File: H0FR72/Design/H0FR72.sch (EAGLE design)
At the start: 38 parts, among them P2 HEXABIT_17.32_NO_P6_P7_P12, Q2 STD36P4LLF6, Q3 MMBT3904LT1, U1 STM32G0B1CEU6NUFQFPN48_STM32_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, U2 INA199A2DCKT, U3 PMD3001D,115, X1 XTALL_CSTCE8M00G52

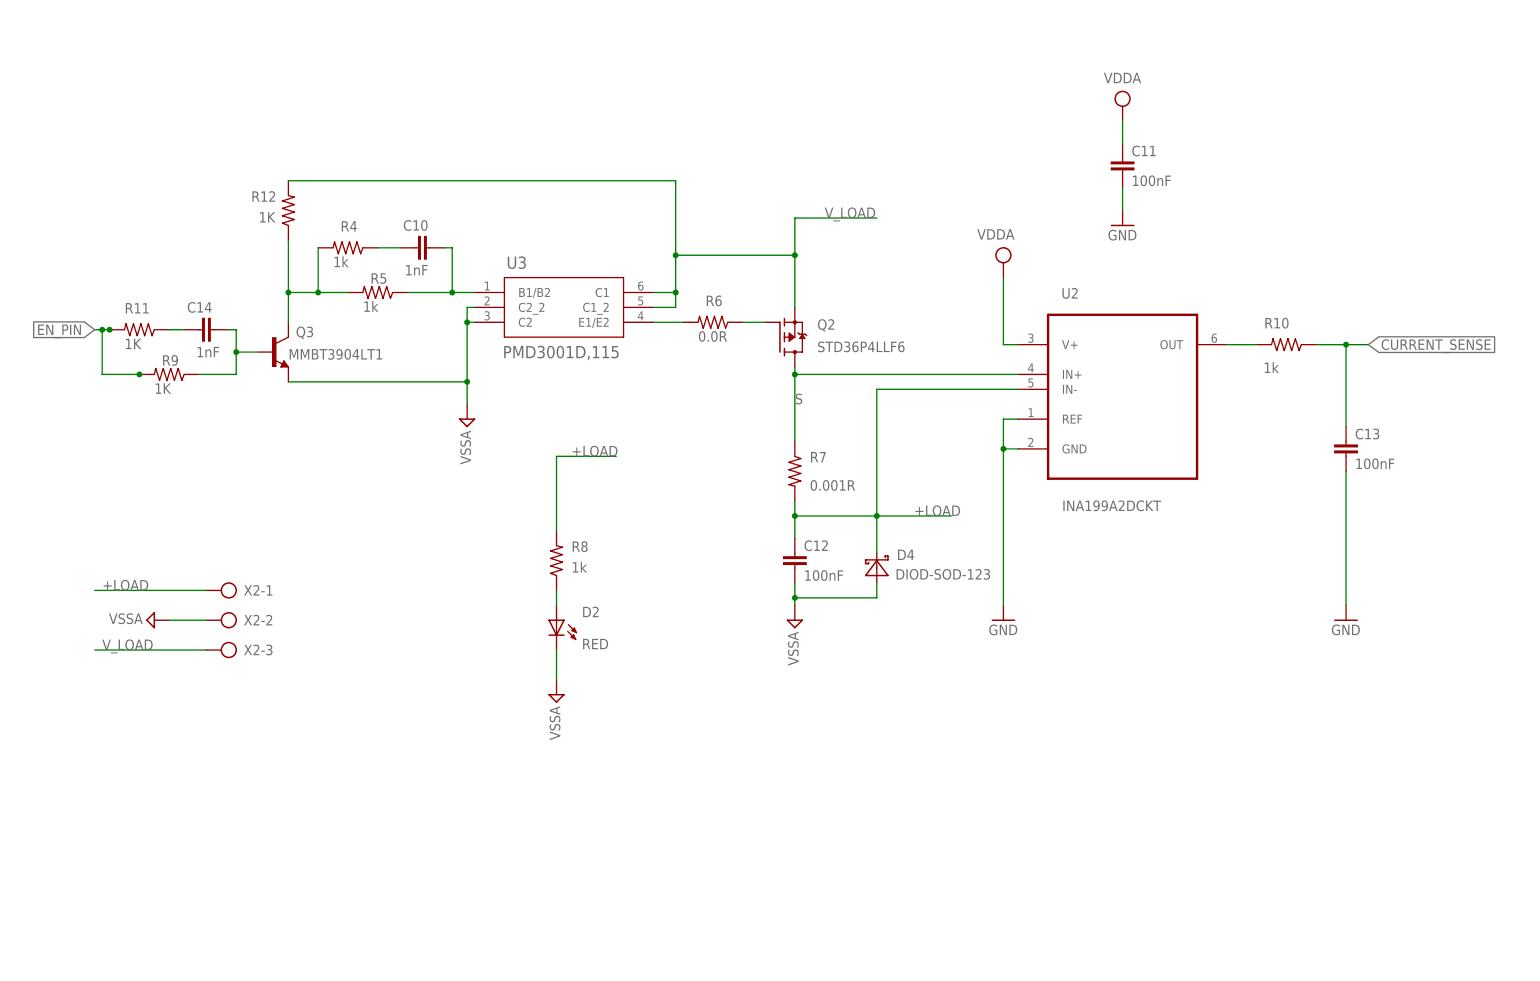
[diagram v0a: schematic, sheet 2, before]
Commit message: -Update the electronic & layout designs to improve the performance (the BOM have been changed too) .
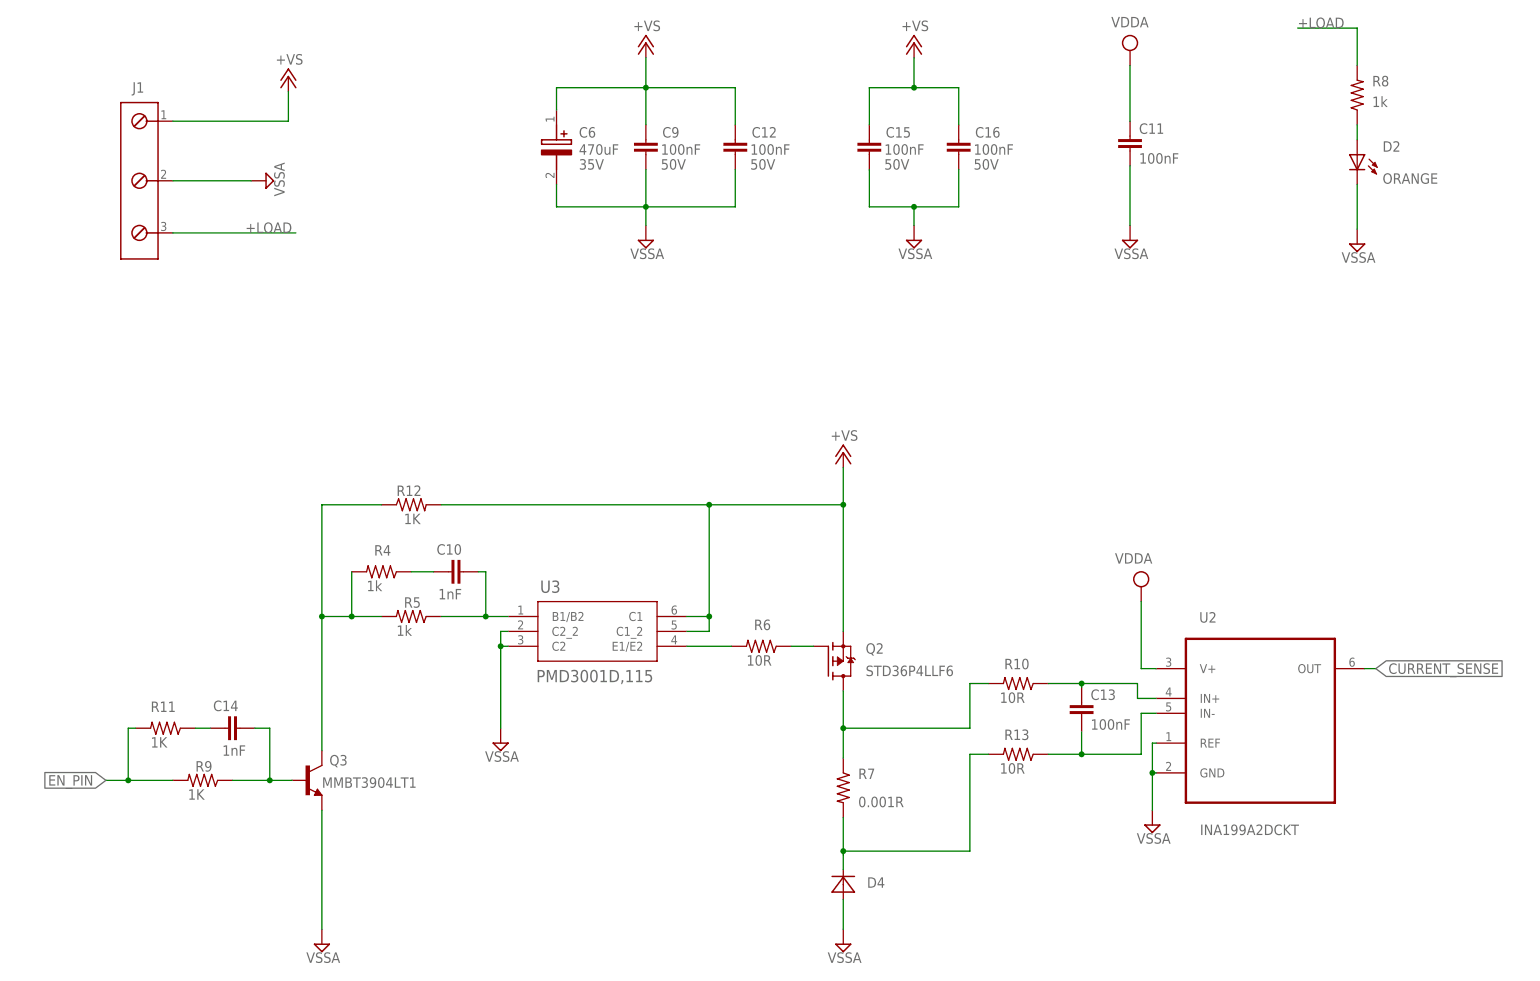
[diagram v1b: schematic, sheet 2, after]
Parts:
- removed JP2: (no value), pinhead:PINHD-1X3
- removed X2: (no value), HEXABITZ_CONNECTION_PARTS:AK500/3
- added C15, C16, C9: (no value), HEXABITZ_RCLS:C-0402
- added C6: ESH477M035AH3AA, HEXABITZ_RCLS:ESH477M035AH3AA
- added J1: (no value), HEXABITZ_CONNECTION_PARTS:691213710003
- added R13: 10R, HEXABITZ_RCLS:R-0402
- added SWD: (no value), HEXABITZ_CONNECTION_PARTS:PINHD-1X3SWD
- C1, C10, C11, C14, C3, C5, C8: device HEXABITZ_RCLS:C-0603 -> HEXABITZ_RCLS:C-0402
- C12: value 100nF -> (none); device HEXABITZ_RCLS:C-0603 -> HEXABITZ_RCLS:C-0402; MFN KEMET -> (none); MPN C0603C104K8RACTU -> (none); OCTOPART_URL https://octopart.com/c0603c104k8ractu-kemet-145075?r=sp&s=9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 -> (none); TOLERANCE 10% -> (none); VOLTAGE_RATING 10V -> 50V
- C13: device HEXABITZ_RCLS:C-0603 -> HEXABITZ_RCLS:C-0402; TOLERANCE 10% -> 10V; VOLTAGE_RATING 10V -> 10%
- C2, C4, C7: device HEXABITZ_RCLS:C-0805-POL -> HEXABITZ_RCLS:C-0603-POL
- D2: value RED -> ORANGE
- R1, R11, R12, R2, R3, R4, R5, R8, R9: device HEXABITZ_RCLS:R-0603 -> HEXABITZ_RCLS:R-0402
- R10: value 1k -> 10R; device HEXABITZ_RCLS:R-0603 -> HEXABITZ_RCLS:R-0402; TOLERANCE 5% -> 1%
- R6: value 0.0R -> 10R; device HEXABITZ_RCLS:R-0603 -> HEXABITZ_RCLS:R-0402
- R7: device HEXABITZ_RCLS:R-US_R2512 -> HEXABITZ_RCLS:R_1206R1206; MPN (none) -> PA1206FRM470R01L
- RESET: value (none) -> R
- U1: value STM32G0B1CEU6NUFQFPN48_STM32_STM -> STM32G0B1CEU6N; device HEXABITZ_ICs:STM32G0B1CEU6NUFQFPN48_STM32_STM -> HEXABITZ_ICs:STM32G0B1CEU6N
- U3: device PMD3001D,115:PMD3001DSOT457_NEX -> HEXABITZ_ICs:PMD3001DSOT457_NEX
- renumbered R to RESET
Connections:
- removed net AGND: C1.2, C12.2, C2.-, C5.2, C7.-, D2.C, D4.A, Q3.E, R2.2, U1.VSS/VSSA, U3.C2, U3.C2_2, X2-2.KL
- removed net N$9: R10.2, U2.OUT
- removed net S: Q2.D, R7.1, U2.IN+
- removed net UART4_RX: P2.SD1, U1.PA1
- removed net UART4_TX: P2.SU1, U1.PA0
- removed net V_LOAD: Q2.S, R12.2, U3.C1, U3.C1_2, X2-3.KL
- new net +VS: C12.2, C15.2, C16.2, C6.+, C9.2, J1.1, Q2.S, R12.2, U3.C1, U3.C1_2
- new net CS: Q2.D, R10.2, R7.1
- new net N$11: C13.1, R10.1, U2.IN+
- new net N$18: C13.2, R13.1, U2.IN-
- new net UART1_RX: P2.SD2, U1.PA9
- new net UART1_TX: P2.SU2, U1.PA10
- new net VREF: C1.1, C2.1, U1.VREF+
- new net VSSA: C1.2, C11.2, C12.1, C15.1, C16.1, C2.2, C5.2, C6.-, C7.2, C9.1, D2.C, D4.A, J1.2, Q3.E, R2.2, U1.VSS/VSSA, U2.GND, U2.REF, U3.C2, U3.C2_2
- net +LOAD: now also J1.3, R13.2; no longer C12.1, U2.IN-, X2-1.KL
- net CLK: now also SWD.1, SWD.2; no longer JP2.1, JP2.2
- net CURRENT_SENSE: now also U1.PA0, U2.OUT; no longer C13.1, R10.1, U1.PB12
- net DATA: now also SWD.3; no longer JP2.3
- net EN_PIN: now also U1.PD1; no longer U1.PB6
- net GND: now also C4.2, U1.PB12, U1.PB13; no longer C11.2, C13.2, C4.-, U1.PB0, U1.PB1, U1.PB7, U1.PB8, U1.PB9, U2.GND, U2.REF
- net N$3: now also U1.PA4; no longer U1.PB13
- net UART2_RX: now also P2.SD5; no longer P2.SD2
- net UART2_TX: now also P2.SU5; no longer P2.SU2
- net UART3_RX: now also P2.SD1; no longer P2.SD4
- net UART3_TX: now also P2.SU1; no longer P2.SU4
- net UART5_RX: now also P2.SD3; no longer P2.SD5
- net UART5_TX: now also P2.SU3; no longer P2.SU5
- net UART6_RX: now also P2.SD4, U1.PB9; no longer P2.SD3, U1.PA5
- net UART6_TX: now also P2.SU4, U1.PB8; no longer P2.SU3, U1.PA4
- net VDD: now also C4.1; no longer C4.+
- net VDDA: now also C7.1; no longer C1.1, C2.+, C7.+, U1.VBAT, U1.VREF+
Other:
- note added: "Current-Shunt Monitor"
- note added: "Driver Output Led_Ind"
- note added: "Driver Power Coupling"
- note added: "Gain = 100 V/V Gain Error = 0.89%"
- note added: "H0FR72"
- note added: "H0FR72_Backend"
- note added: "H0FR72_Frontend"
- note added: "Input Power Coupling"
- note added: "Load driver"
- note added: "U2 Coupling"
- note added: "VS=(3.3-18) Volts"
- note removed: "H0FR71"
- note removed: "H0FR71_Backend"
- note removed: "H0FR71_Frontend"
- note removed: "V_load=(3.3-18)"
- moved on the sheet: C10, C11, C12, C13, C14, D1, D2, Q2, Q3, R1, R10, R11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

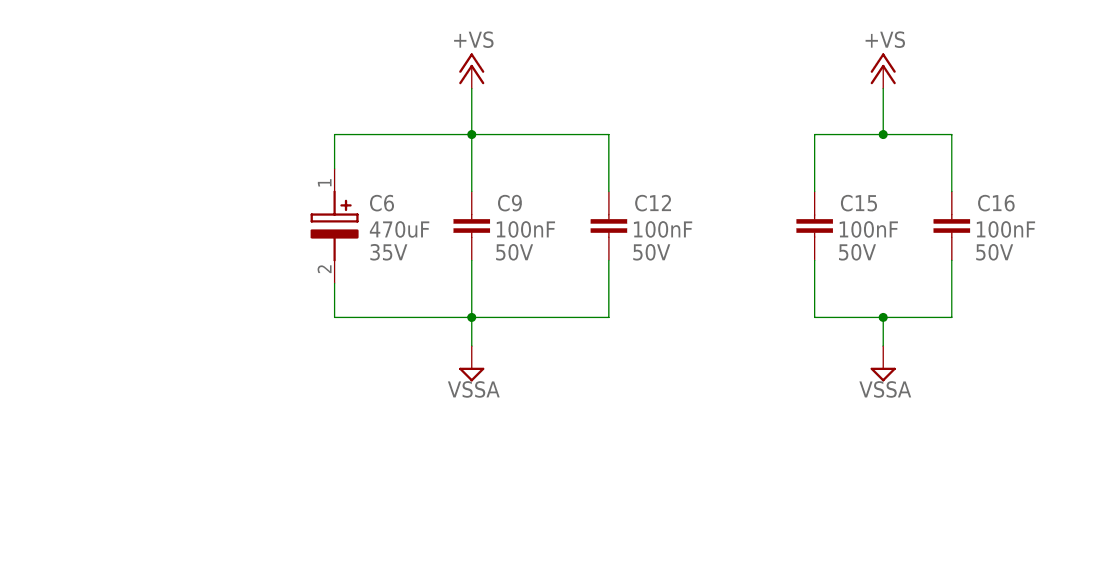
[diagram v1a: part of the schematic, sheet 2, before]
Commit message: -Add additional 10u capacitor to gate driver IC supply
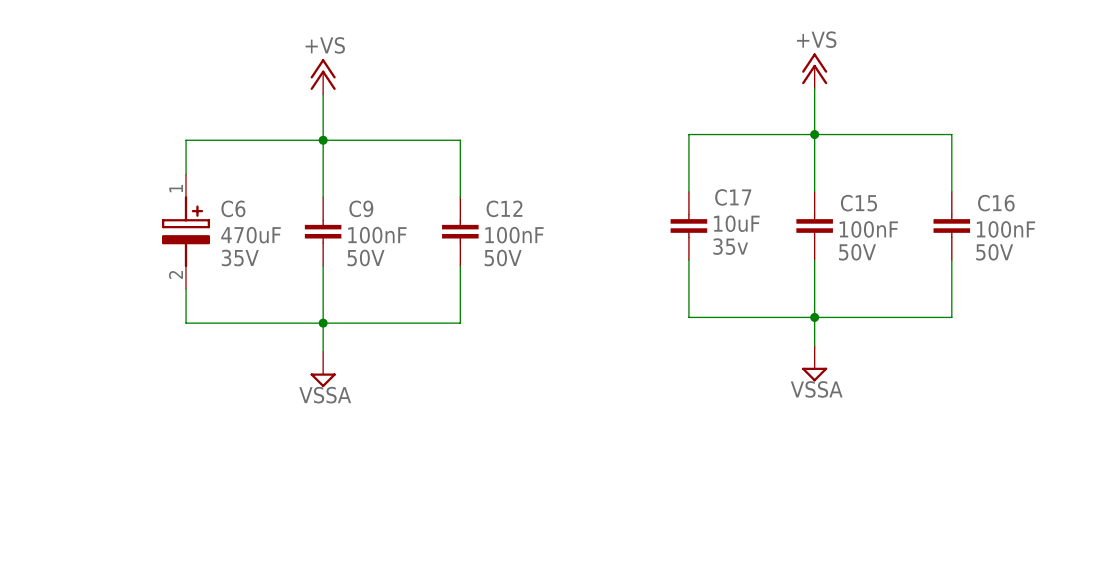
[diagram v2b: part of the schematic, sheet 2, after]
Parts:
- added C17: C-0805, HEXABITZ_RCLS:C-0805
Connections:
- net +VS: now also C17.1
- net VSSA: now also C17.2
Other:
- moved on the sheet: C12, C6, C9
